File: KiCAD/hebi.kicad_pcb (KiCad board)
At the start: 4 copper layers, 49 x 49 mm, 110 parts, among them K1 CONN_3, K2 CONN_3, K3 CONN_3, K4 CONN_3, K5 CONN_3, P1 CONN_4, P2 CONN_4, P3 CONN_4, P4 CONN_4, P6 CONN_2, Q1 MOS_N_DIODE, Q10 MOS_N_DIODE, Q2 MOS_N_DIODE, Q3 MOS_N_DIODE, Q4 MOS_N_DIODE, Q5 MOS_N_DIODE, Q6 MOS_N_DIODE, Q7 MOS_N_DIODE, Q9 MOS_N_DIODE, SW1 SW_PUSH, SW2 SW_PUSH, SW3 SW_PUSH, U1 MPU-6050, U2 HMC5883L, U3 MCP1825S, U4 STM32F407VG, U5 XBEE, X1 8MHz

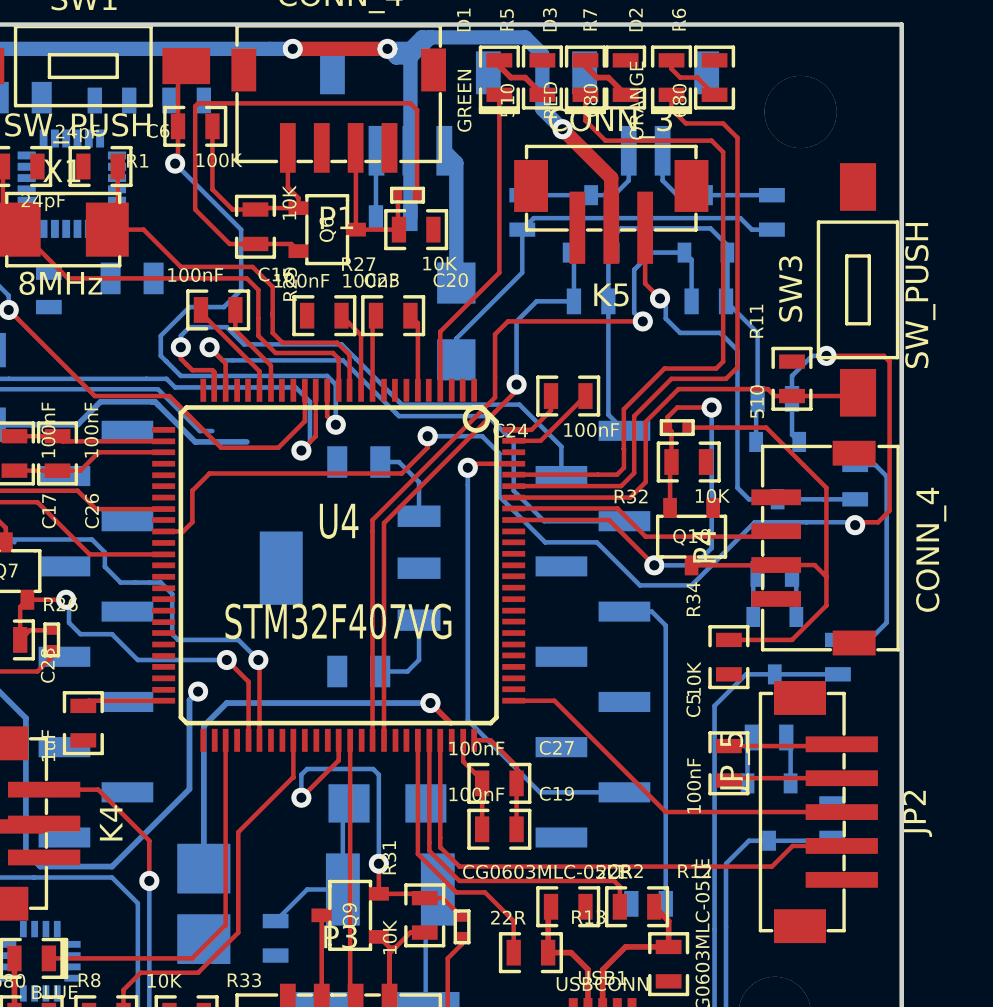
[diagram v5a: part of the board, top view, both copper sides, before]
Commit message: Added even more tracks.
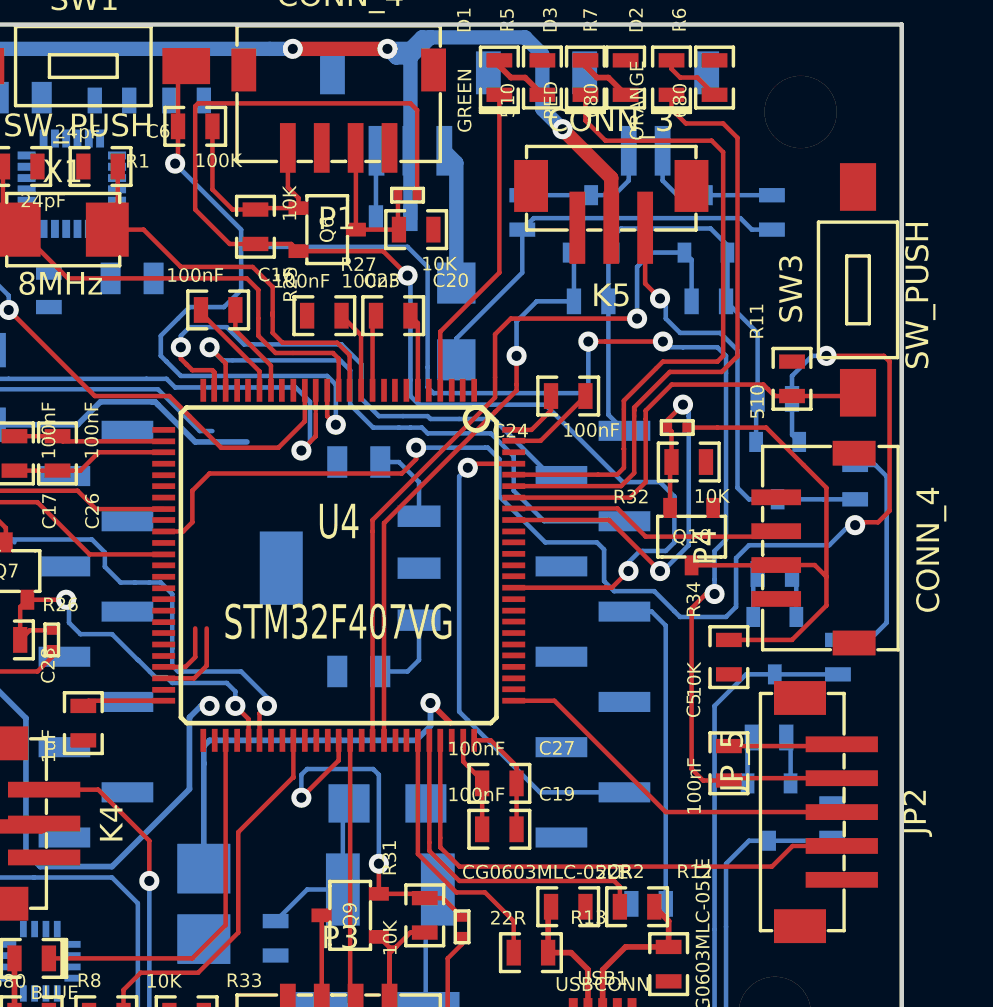
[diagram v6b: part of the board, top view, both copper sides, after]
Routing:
- net /RESET: track 33.4 -> 84.1 mm, vias 2 -> 5
- net /TX1_3V: track 23.7 -> 58.1 mm, vias 0 -> 2
- net /I2C_PCB_SDA: track 0.00 -> 3.79 mm
- net /I2C_PCB_SCL: track 0.00 -> 2.85 mm
- net /SERVO3_3V: track 54.8 -> 57.3 mm
- net /TX4_3V: track 22.4 -> 20.4 mm
- net /TX3_3V: track 17.9 -> 17.3 mm
- net /I2C_SDA_PWR_3V: track 34.3 -> 33.7 mm
- net /XBEE_RX: track 25.0 -> 25.5 mm

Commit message: Routed even more things.
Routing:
- net /RX1: track 0.00 -> 24.0 mm, vias 0 -> 2
- net /VBUS: track 5.56 -> 14.3 mm, vias 0 -> 1
- net /XBEE_TX: track 25.0 -> 32.8 mm
- net /XBEE_RX: track 25.5 -> 33.3 mm
- net N-0000045: track 15.9 -> 18.0 mm, vias 0 -> 1
- net N-0000046: track 23.1 -> 25.0 mm, vias 0 -> 1
- net /TX1_3V: track 58.1 -> 60.0 mm
- net N-0000042: track 23.0 -> 24.7 mm
- net /RESET: track 84.1 -> 85.0 mm
- net /XBEE_SLEEP: track 21.9 -> 21.0 mm
- net /ADC1: track 29.4 -> 28.5 mm
- net /SERVO3_3V: track 57.3 -> 58.1 mm
- net /ADC2: track 24.2 -> 24.7 mm

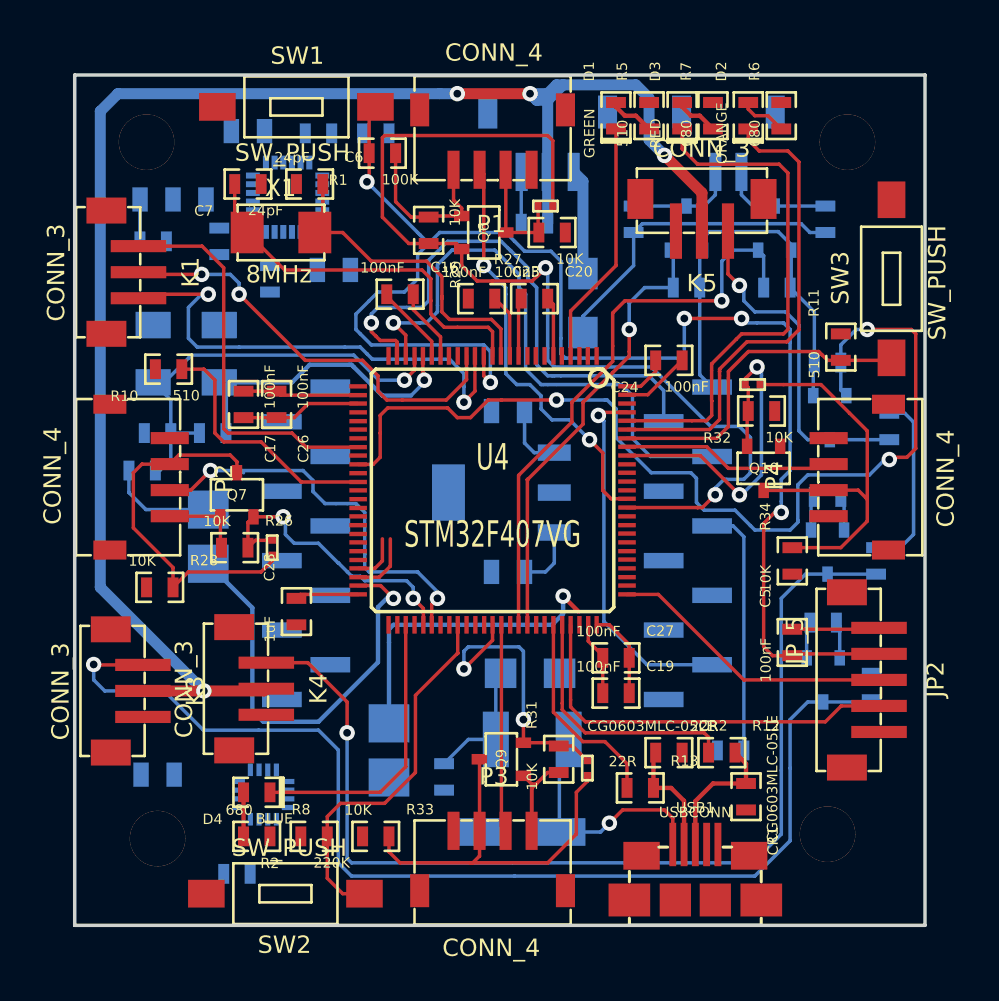
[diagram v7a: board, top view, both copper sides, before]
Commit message: Routed power tracks, removed IMU.
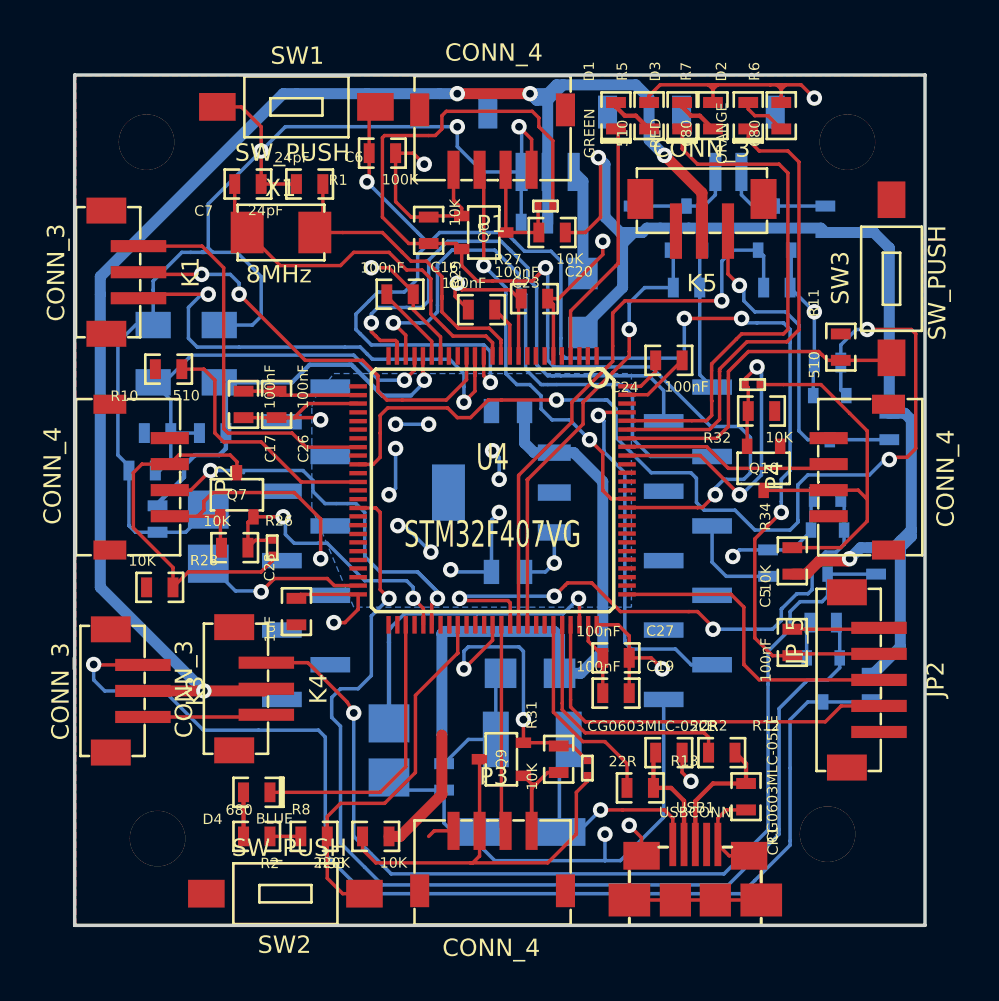
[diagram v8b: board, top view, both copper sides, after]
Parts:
- removed C1, C3: 0.1uF, SM0603_Opendous(generic)
- removed C14: 220nF, SM0603_Opendous(generic)
- removed C2: 10nF, SM0805_Opendous(generic)
- removed C4: 2.2nF, SM0805_Opendous(generic)
- removed C8: 4.7uF, SM0805_Opendous(generic)
- removed JP1: JUMPER3, 0805_Jumper
- removed R4, R9: 4.7K, SM0603_Opendous(generic)
- removed U1: MPU-6050, MPU-6050
- removed U2: HMC5883L, HMC58583L-hebi
- moved C12 16.0 mm to (178.6, 137.3), turned to 270 degrees
- moved R14 11.0 mm to (213.7, 139.8), turned to 270 degrees
- moved C23 0.63 mm to (197.2, 125.2)
- turned R33 to 180 degrees
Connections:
- U4 pad 2: /ACCEL_INT -> N-0000087
- U4 pad 47: /I2C_PCB_SCL -> N-0000088
- U4 pad 48: /I2C_PCB_SDA -> N-0000089
- U4 pad 98: /COMPASS_INT -> N-0000086
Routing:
- net GND: track 39.7 -> 218.7 mm, vias 0 -> 18
- net +5V: track 32.8 -> 116.3 mm, vias 0 -> 2
- net /SERVO1_3V: track 2.11 -> 64.7 mm, vias 0 -> 1
- net /SERVO2_3V: track 1.98 -> 34.0 mm, vias 0 -> 3
- net VCC: track 84.0 -> 110.9 mm, vias 0 -> 10
- net N-000004: track 24.7 -> 9.79 mm
- net /XBEE_RESET: track 14.4 -> 5.65 mm
- net N-000002: track 18.0 -> 24.6 mm
- net /SERVO_PWR: track 106.7 -> 101.2 mm
- net /I2C_PCB_SDA: track 3.69 -> 0.00 mm
- net /I2C_PCB_SCL: track 2.85 -> 0.00 mm
- net /SWCLK: track 16.6 -> 18.5 mm
- net /TX1_3V: track 60.0 -> 61.9 mm
- net /TX2: track 22.6 -> 24.0 mm
- net /RX3: track 23.4 -> 24.7 mm
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- added copper zone on B.Cu, net GND
- added copper zone on Inner2.Cu, net GND
- added copper zone on F.Cu, net VCC
- added copper zone on Inner1.Cu, net VCC
